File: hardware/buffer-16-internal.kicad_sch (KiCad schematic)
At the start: 6 parts, among them U2 74LVC8T245, U3 74LVC8T245

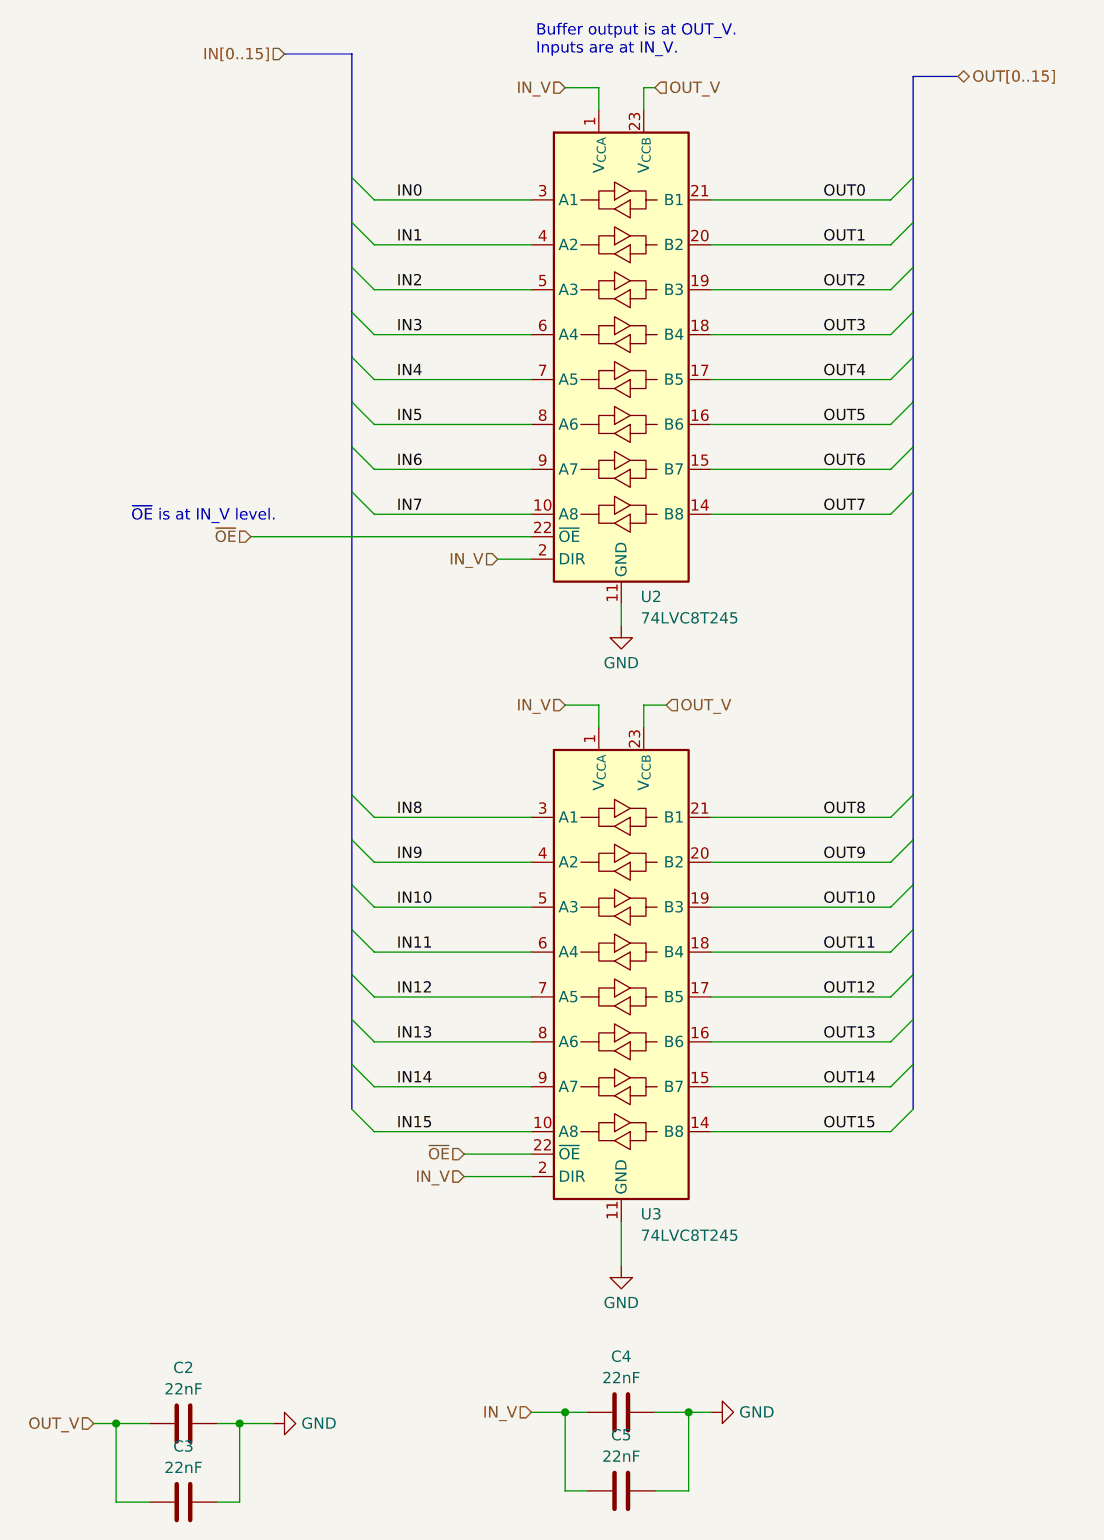
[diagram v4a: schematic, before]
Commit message: Move SRAM bank board design into shareable subsheet
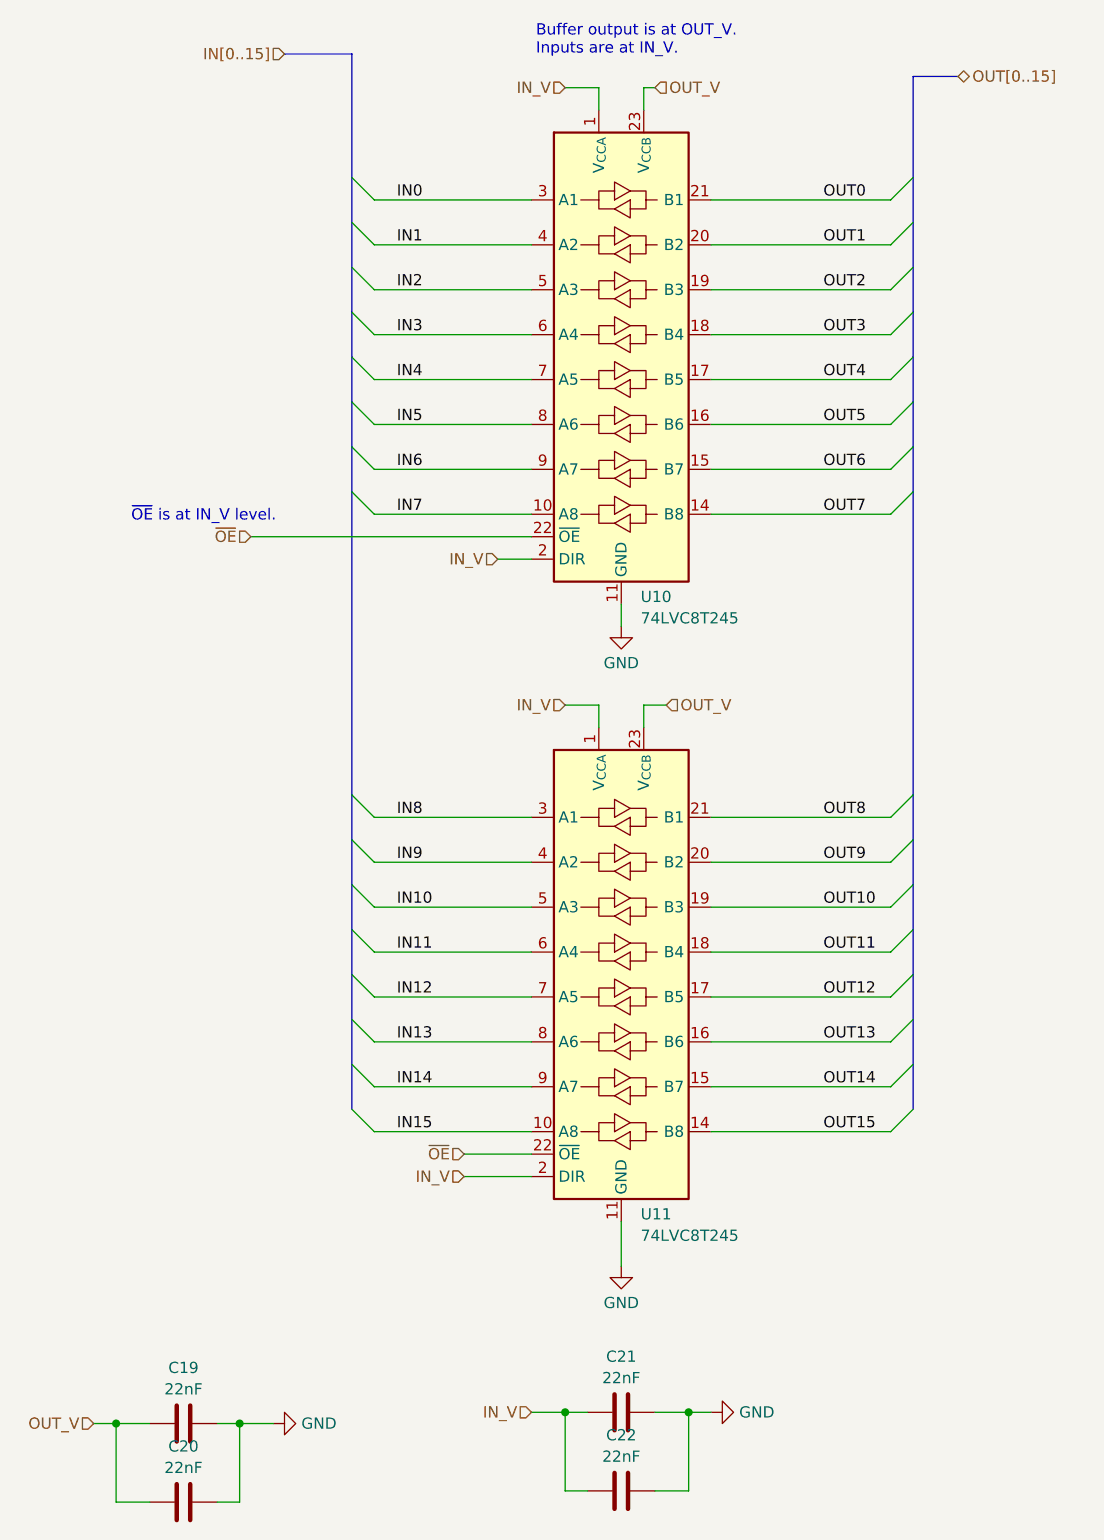
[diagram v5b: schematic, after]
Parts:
- renumbered C2 to C19, C3 to C20, C4 to C21, C5 to C22, U2 to U10, U3 to U11
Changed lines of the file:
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@@
 		(dnp no)
 		(fields_autoplaced yes)
-		(property "Reference" "U2"
+		(property "Reference" "U10"
 			(at 129.1941 84.2701 0)
 			(effects
@@
 		(instances
 			(project "sram-bank"
-				(path "/620c762c-1ae9-4ea9-ab1a-d023a8da85ac/7fd3a89c-21a0-42ad-aeef-3acbc5a82fbe"
-					(reference "U4")
-					(unit 1)
-				)
-				(path "/620c762c-1ae9-4ea9-ab1a-d023a8da85ac/96cb94ae-287c-4ad3-afb4-5a50560014d1"
-					(reference "U2")
+				(path "/620c762c-1ae9-4ea9-ab1a-d023a8da85ac/de6964c0-b8e7-4813-9bb5-2e4faf4431cb/0a8080e9-a039-47f4-ae61-d3888692a6ad"
+					(reference "U8")
+					(unit 1)
+				)
+				(path "/620c762c-1ae9-4ea9-ab1a-d023a8da85ac/de6964c0-b8e7-4813-9bb5-2e4faf4431cb/8fba2bc8-5b90-4ec8-a637-aa04f63ad055"
+					(reference "U10")
 					(unit 1)
 				)
@@
 		(dnp no)
 		(fields_autoplaced yes)
-		(property "Reference" "#PWR038"
+		(property "Reference" "#PWR032"
 			(at 127 166.37 0)
 			(effects
@@
 		(instances
 			(project "sram-bank"
-				(path "/620c762c-1ae9-4ea9-ab1a-d023a8da85ac/7fd3a89c-21a0-42ad-aeef-3acbc5a82fbe"
-					(reference "#PWR039")
-					(unit 1)
-				)
-				(path "/620c762c-1ae9-4ea9-ab1a-d023a8da85ac/96cb94ae-287c-4ad3-afb4-5a50560014d1"
-					(reference "#PWR038")
+				(path "/620c762c-1ae9-4ea9-ab1a-d023a8da85ac/de6964c0-b8e7-4813-9bb5-2e4faf4431cb/0a8080e9-a039-47f4-ae61-d3888692a6ad"
+					(reference "#PWR028")
+					(unit 1)
+				)
+				(path "/620c762c-1ae9-4ea9-ab1a-d023a8da85ac/de6964c0-b8e7-4813-9bb5-2e4faf4431cb/8fba2bc8-5b90-4ec8-a637-aa04f63ad055"
+					(reference "#PWR032")
 					(unit 1)
 				)
@@
 		(dnp no)
 		(fields_autoplaced yes)
-		(property "Reference" "C4"
+		(property "Reference" "C21"
 			(at 127 170.2265 90)
 			(effects
@@
 		(instances
 			(project "sram-bank"
-				(path "/620c762c-1ae9-4ea9-ab1a-d023a8da85ac/7fd3a89c-21a0-42ad-aeef-3acbc5a82fbe"
-					(reference "C8")
-					(unit 1)
-				)
-				(path "/620c762c-1ae9-4ea9-ab1a-d023a8da85ac/96cb94ae-287c-4ad3-afb4-5a50560014d1"
-					(reference "C4")
+				(path "/620c762c-1ae9-4ea9-ab1a-d023a8da85ac/de6964c0-b8e7-4813-9bb5-2e4faf4431cb/0a8080e9-a039-47f4-ae61-d3888692a6ad"
+					(reference "C17")
+					(unit 1)
+				)
+				(path "/620c762c-1ae9-4ea9-ab1a-d023a8da85ac/de6964c0-b8e7-4813-9bb5-2e4faf4431cb/8fba2bc8-5b90-4ec8-a637-aa04f63ad055"
+					(reference "C21")
 					(unit 1)
 				)
@@
 		(dnp no)
 		(fields_autoplaced yes)
-		(property "Reference" "#PWR040"
+		(property "Reference" "#PWR030"
 			(at 93.98 177.8 0)
 			(effects
@@
 		(instances
 			(project "sram-bank"
-				(path "/620c762c-1ae9-4ea9-ab1a-d023a8da85ac/7fd3a89c-21a0-42ad-aeef-3acbc5a82fbe"
-					(reference "#PWR041")
-					(unit 1)
-				)
-				(path "/620c762c-1ae9-4ea9-ab1a-d023a8da85ac/96cb94ae-287c-4ad3-afb4-5a50560014d1"
-					(reference "#PWR040")
+				(path "/620c762c-1ae9-4ea9-ab1a-d023a8da85ac/de6964c0-b8e7-4813-9bb5-2e4faf4431cb/0a8080e9-a039-47f4-ae61-d3888692a6ad"
+					(reference "#PWR026")
+					(unit 1)
+				)
+				(path "/620c762c-1ae9-4ea9-ab1a-d023a8da85ac/de6964c0-b8e7-4813-9bb5-2e4faf4431cb/8fba2bc8-5b90-4ec8-a637-aa04f63ad055"
+					(reference "#PWR030")
 					(unit 1)
 				)
@@
 		(dnp no)
 		(fields_autoplaced yes)
-		(property "Reference" "C3"
+		(property "Reference" "C20"
 			(at 77.47 180.3865 90)
 			(effects
@@
 		(instances
 			(project "sram-bank"
-				(path "/620c762c-1ae9-4ea9-ab1a-d023a8da85ac/7fd3a89c-21a0-42ad-aeef-3acbc5a82fbe"
-					(reference "C7")
-					(unit 1)
-				)
-				(path "/620c762c-1ae9-4ea9-ab1a-d023a8da85ac/96cb94ae-287c-4ad3-afb4-5a50560014d1"
-					(reference "C3")
+				(path "/620c762c-1ae9-4ea9-ab1a-d023a8da85ac/de6964c0-b8e7-4813-9bb5-2e4faf4431cb/0a8080e9-a039-47f4-ae61-d3888692a6ad"
+					(reference "C16")
+					(unit 1)
+				)
+				(path "/620c762c-1ae9-4ea9-ab1a-d023a8da85ac/de6964c0-b8e7-4813-9bb5-2e4faf4431cb/8fba2bc8-5b90-4ec8-a637-aa04f63ad055"
+					(reference "C20")
 					(unit 1)
 				)
@@
 		(dnp no)
 		(fields_autoplaced yes)
-		(property "Reference" "C2"
+		(property "Reference" "C19"
 			(at 77.47 171.4965 90)
 			(effects
@@
 		(instances
 			(project "sram-bank"
-				(path "/620c762c-1ae9-4ea9-ab1a-d023a8da85ac/7fd3a89c-21a0-42ad-aeef-3acbc5a82fbe"
-					(reference "C6")
-					(unit 1)
-				)
-				(path "/620c762c-1ae9-4ea9-ab1a-d023a8da85ac/96cb94ae-287c-4ad3-afb4-5a50560014d1"
-					(reference "C2")
+				(path "/620c762c-1ae9-4ea9-ab1a-d023a8da85ac/de6964c0-b8e7-4813-9bb5-2e4faf4431cb/0a8080e9-a039-47f4-ae61-d3888692a6ad"
+					(reference "C15")
+					(unit 1)
+				)
+				(path "/620c762c-1ae9-4ea9-ab1a-d023a8da85ac/de6964c0-b8e7-4813-9bb5-2e4faf4431cb/8fba2bc8-5b90-4ec8-a637-aa04f63ad055"
+					(reference "C19")
 					(unit 1)
 				)
@@
 		(dnp no)
 		(fields_autoplaced yes)
-		(property "Reference" "#PWR042"
+		(property "Reference" "#PWR033"
 			(at 143.51 176.53 0)
 			(effects
@@
 		(instances
 			(project "sram-bank"
-				(path "/620c762c-1ae9-4ea9-ab1a-d023a8da85ac/7fd3a89c-21a0-42ad-aeef-3acbc5a82fbe"
-					(reference "#PWR043")
-					(unit 1)
-				)
-				(path "/620c762c-1ae9-4ea9-ab1a-d023a8da85ac/96cb94ae-287c-4ad3-afb4-5a50560014d1"
-					(reference "#PWR042")
+				(path "/620c762c-1ae9-4ea9-ab1a-d023a8da85ac/de6964c0-b8e7-4813-9bb5-2e4faf4431cb/0a8080e9-a039-47f4-ae61-d3888692a6ad"
+					(reference "#PWR029")
+					(unit 1)
+				)
+				(path "/620c762c-1ae9-4ea9-ab1a-d023a8da85ac/de6964c0-b8e7-4813-9bb5-2e4faf4431cb/8fba2bc8-5b90-4ec8-a637-aa04f63ad055"
+					(reference "#PWR033")
 					(unit 1)
 				)
@@
 		(dnp no)
 		(fields_autoplaced yes)
-		(property "Reference" "C5"
+		(property "Reference" "C22"
 			(at 127 179.1165 90)
 			(effects
@@
 		(instances
 			(project "sram-bank"
-				(path "/620c762c-1ae9-4ea9-ab1a-d023a8da85ac/7fd3a89c-21a0-42ad-aeef-3acbc5a82fbe"
-					(reference "C9")
-					(unit 1)
-				)
-				(path "/620c762c-1ae9-4ea9-ab1a-d023a8da85ac/96cb94ae-287c-4ad3-afb4-5a50560014d1"
-					(reference "C5")
+				(path "/620c762c-1ae9-4ea9-ab1a-d023a8da85ac/de6964c0-b8e7-4813-9bb5-2e4faf4431cb/0a8080e9-a039-47f4-ae61-d3888692a6ad"
+					(reference "C18")
+					(unit 1)
+				)
+				(path "/620c762c-1ae9-4ea9-ab1a-d023a8da85ac/de6964c0-b8e7-4813-9bb5-2e4faf4431cb/8fba2bc8-5b90-4ec8-a637-aa04f63ad055"
+					(reference "C22")
 					(unit 1)
 				)
@@
 		(dnp no)
 		(fields_autoplaced yes)
-		(property "Reference" "U3"
+		(property "Reference" "U11"
 			(at 129.1941 154.1201 0)
 			(effects
@@
 		(instances
 			(project "sram-bank"
-				(path "/620c762c-1ae9-4ea9-ab1a-d023a8da85ac/7fd3a89c-21a0-42ad-aeef-3acbc5a82fbe"
-					(reference "U5")
-					(unit 1)
-				)
-				(path "/620c762c-1ae9-4ea9-ab1a-d023a8da85ac/96cb94ae-287c-4ad3-afb4-5a50560014d1"
-					(reference "U3")
+				(path "/620c762c-1ae9-4ea9-ab1a-d023a8da85ac/de6964c0-b8e7-4813-9bb5-2e4faf4431cb/0a8080e9-a039-47f4-ae61-d3888692a6ad"
+					(reference "U9")
+					(unit 1)
+				)
+				(path "/620c762c-1ae9-4ea9-ab1a-d023a8da85ac/de6964c0-b8e7-4813-9bb5-2e4faf4431cb/8fba2bc8-5b90-4ec8-a637-aa04f63ad055"
+					(reference "U11")
 					(unit 1)
 				)
@@
 		(dnp no)
 		(fields_autoplaced yes)
-		(property "Reference" "#PWR036"
+		(property "Reference" "#PWR031"
 			(at 127 93.98 0)
 			(effects
@@
 		(instances
 			(project "sram-bank"
-				(path "/620c762c-1ae9-4ea9-ab1a-d023a8da85ac/7fd3a89c-21a0-42ad-aeef-3acbc5a82fbe"
-					(reference "#PWR037")
-					(unit 1)
-				)
-				(path "/620c762c-1ae9-4ea9-ab1a-d023a8da85ac/96cb94ae-287c-4ad3-afb4-5a50560014d1"
-					(reference "#PWR036")
-					(unit 1)
-				)
+				(path "/620c762c-1ae9-4ea9-ab1a-d023a8da85ac/de6964c0-b8e7-4813-9bb5-2e4faf4431cb/0a8080e9-a039-47f4-ae61-d3888692a6ad"
+					(reference "#PWR027")
+					(unit 1)
+				)
+				(path "/620c762c-1ae9-4ea9-ab1a-d023a8da85ac/de6964c0-b8e7-4813-9bb5-2e4faf4431cb/8fba2bc8-5b90-4ec8-a637-aa04f63ad055"
+					(reference "#PWR031")
+					(unit 1)
+				)

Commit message: Reannotate schematics and drop debug bridges
Parts are now numbered starting at 0 for cart, 100 for SRAM, 300 for
microcontroller.

Also, drop debug bridges that made routing more difficult and had the
same names across prototype boards.

Hopefully this will help avoid naming conflicts for the unified PCB.

Also, redo prototype PCB layouts.

Now that all the names have changed, update board layouts.
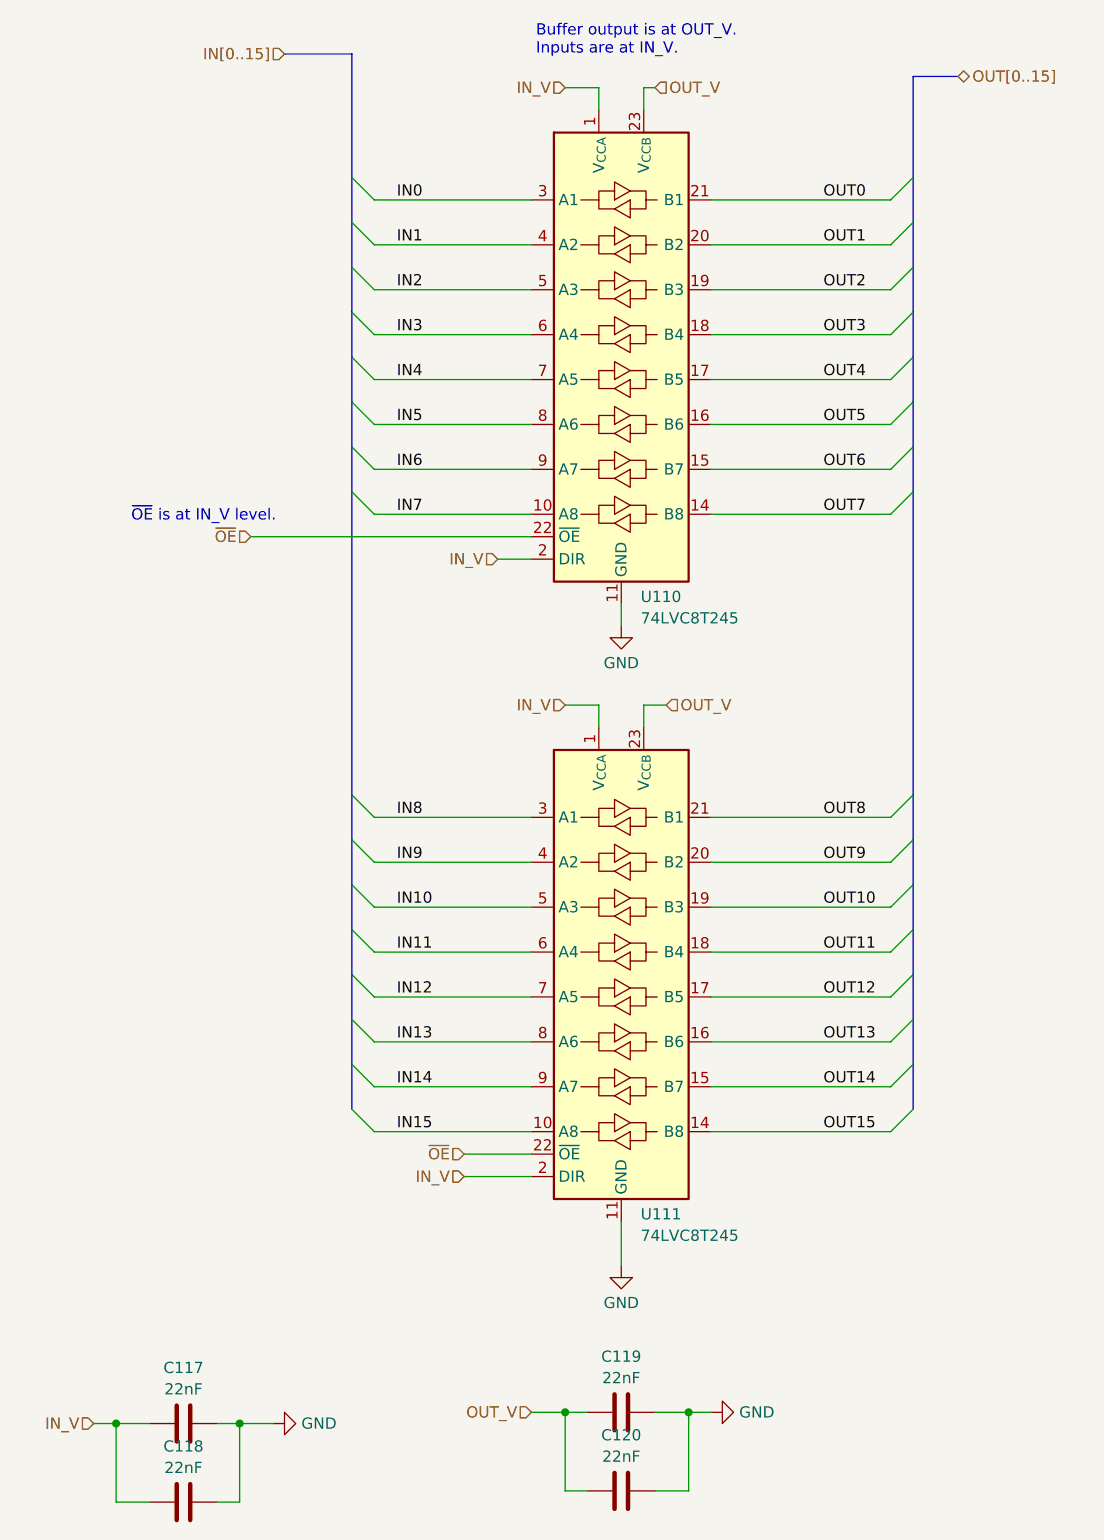
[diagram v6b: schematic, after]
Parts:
- renumbered C19 to C117, C20 to C118, C21 to C119, C22 to C120, U10 to U110, U11 to U111
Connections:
- net IN_V: now also C117.1, C118.1; no longer C119.1, C120.1
- net OUT_V: now also C119.1, C120.1; no longer C117.1, C118.1
